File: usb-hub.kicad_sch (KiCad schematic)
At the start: 17 parts, among them U5 CH334P, Y2 X322512MSB4SI

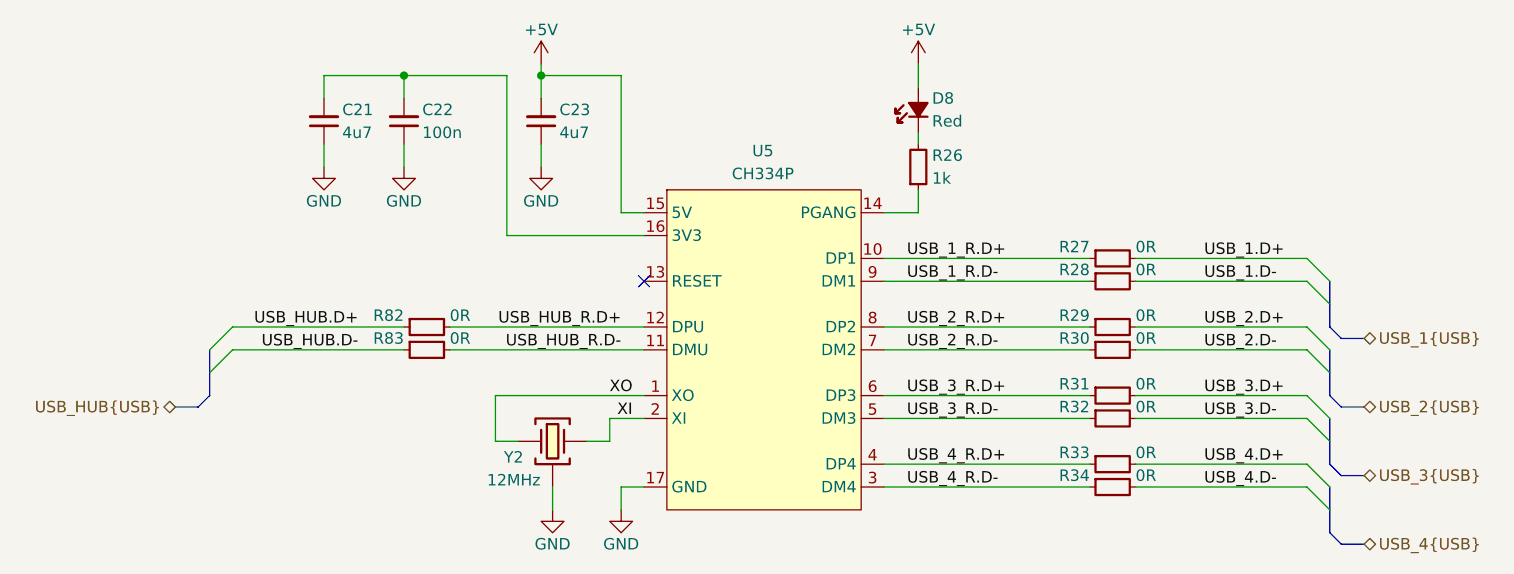
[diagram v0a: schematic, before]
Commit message: [#3] WIP: Clear ERC, re-annotate schematic
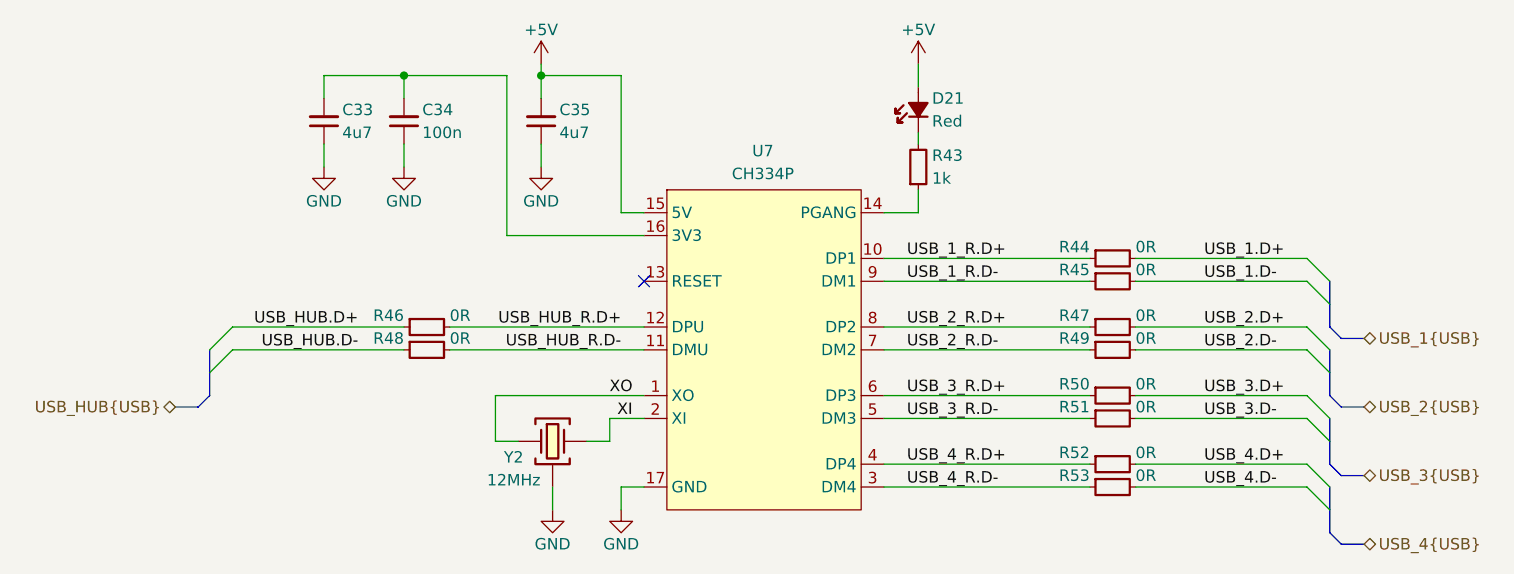
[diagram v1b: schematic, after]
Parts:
- renumbered C21 to C33, C22 to C34, C23 to C35, D8 to D21, R26 to R43, R27 to R44, R28 to R45, R82 to R46, R29 to R47, R83 to R48, R30 to R49, R31 to R50, R32 to R51, R33 to R52, R34 to R53, U5 to U7
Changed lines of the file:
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@@
 		(on_board yes)
 		(dnp no)
-		(property "Reference" "D8"
+		(property "Reference" "D21"
 			(at 164.084 80.01 90)
 			(effects
@@
 			(project "cm5-module"
 				(path "/090a8e41-87a8-4fb1-998b-60a2c0dc4cee/4f95f4d3-6409-4bd0-9a25-1272a43f6549"
-					(reference "D8")
+					(reference "D21")
 					(unit 1)
 				)
@@
 		(on_board yes)
 		(dnp no)
-		(property "Reference" "U5"
+		(property "Reference" "U7"
 			(at 145.288 85.852 0)
 			(effects
@@
 			(project ""
 				(path "/090a8e41-87a8-4fb1-998b-60a2c0dc4cee/4f95f4d3-6409-4bd0-9a25-1272a43f6549"
-					(reference "U5")
+					(reference "U7")
 					(unit 1)
 				)
@@
 		(on_board yes)
 		(dnp no)
-		(property "Reference" "R32"
+		(property "Reference" "R51"
 			(at 181.61 114.3 0)
 			(effects
@@
 			(project "cm5-module"
 				(path "/090a8e41-87a8-4fb1-998b-60a2c0dc4cee/4f95f4d3-6409-4bd0-9a25-1272a43f6549"
-					(reference "R32")
+					(reference "R51")
 					(unit 1)
 				)
@@
 		(on_board yes)
 		(dnp no)
-		(property "Reference" "#PWR070"
+		(property "Reference" "#PWR0108"
 			(at 96.52 93.98 0)
 			(effects
@@
 			(project "cm5-module"
 				(path "/090a8e41-87a8-4fb1-998b-60a2c0dc4cee/4f95f4d3-6409-4bd0-9a25-1272a43f6549"
-					(reference "#PWR070")
+					(reference "#PWR0108")
 					(unit 1)
 				)
@@
 		(on_board yes)
 		(dnp no)
-		(property "Reference" "#PWR073"
+		(property "Reference" "#PWR0111"
 			(at 121.92 132.08 0)
 			(effects
@@
 			(project "cm5-module"
 				(path "/090a8e41-87a8-4fb1-998b-60a2c0dc4cee/4f95f4d3-6409-4bd0-9a25-1272a43f6549"
-					(reference "#PWR073")
+					(reference "#PWR0111")
 					(unit 1)
 				)
@@
 		(on_board yes)
 		(dnp no)
-		(property "Reference" "#PWR071"
+		(property "Reference" "#PWR0109"
 			(at 105.41 93.98 0)
 			(effects
@@
 			(project "cm5-module"
 				(path "/090a8e41-87a8-4fb1-998b-60a2c0dc4cee/4f95f4d3-6409-4bd0-9a25-1272a43f6549"
-					(reference "#PWR071")
+					(reference "#PWR0109")
 					(unit 1)
 				)
@@
 		(on_board yes)
 		(dnp no)
-		(property "Reference" "#PWR074"
+		(property "Reference" "#PWR0112"
 			(at 129.54 132.08 0)
 			(effects
@@
 			(project "cm5-module"
 				(path "/090a8e41-87a8-4fb1-998b-60a2c0dc4cee/4f95f4d3-6409-4bd0-9a25-1272a43f6549"
-					(reference "#PWR074")
+					(reference "#PWR0112")
 					(unit 1)
 				)
@@
 		(on_board yes)
 		(dnp no)
-		(property "Reference" "R29"
+		(property "Reference" "R47"
 			(at 181.61 104.14 0)
 			(effects
@@
 			(project "cm5-module"
 				(path "/090a8e41-87a8-4fb1-998b-60a2c0dc4cee/4f95f4d3-6409-4bd0-9a25-1272a43f6549"
-					(reference "R29")
+					(reference "R47")
 					(unit 1)
 				)
@@
 		(on_board yes)
 		(dnp no)
-		(property "Reference" "R34"
+		(property "Reference" "R53"
 			(at 181.61 121.92 0)
 			(effects
@@
 			(project "cm5-module"
 				(path "/090a8e41-87a8-4fb1-998b-60a2c0dc4cee/4f95f4d3-6409-4bd0-9a25-1272a43f6549"
-					(reference "R34")
+					(reference "R53")
 					(unit 1)
 				)
@@
 		(on_board yes)
 		(dnp no)
-		(property "Reference" "R26"
+		(property "Reference" "R43"
 			(at 164.084 86.36 90)
 			(effects
@@
 			(project "cm5-module"
 				(path "/090a8e41-87a8-4fb1-998b-60a2c0dc4cee/4f95f4d3-6409-4bd0-9a25-1272a43f6549"
-					(reference "R26")
+					(reference "R43")
 					(unit 1)
 				)
@@
 		(on_board yes)
 		(dnp no)
-		(property "Reference" "R28"
+		(property "Reference" "R45"
 			(at 181.61 99.06 0)
 			(effects
@@
 			(project "cm5-module"
 				(path "/090a8e41-87a8-4fb1-998b-60a2c0dc4cee/4f95f4d3-6409-4bd0-9a25-1272a43f6549"
-					(reference "R28")
+					(reference "R45")
 					(unit 1)
 				)
@@
 		(on_board yes)
 		(dnp no)
-		(property "Reference" "C22"
+		(property "Reference" "C34"
 			(at 107.442 81.28 90)
 			(effects
@@
 			(project "cm5-module"
 				(path "/090a8e41-87a8-4fb1-998b-60a2c0dc4cee/4f95f4d3-6409-4bd0-9a25-1272a43f6549"
-					(reference "C22")
+					(reference "C34")
 					(unit 1)
 				)
@@
 		(on_board yes)
 		(dnp no)
-		(property "Reference" "C23"
+		(property "Reference" "C35"
 			(at 122.682 81.28 90)
 			(effects
@@
 			(project ""
 				(path "/090a8e41-87a8-4fb1-998b-60a2c0dc4cee/4f95f4d3-6409-4bd0-9a25-1272a43f6549"
-					(reference "C23")
+					(reference "C35")
 					(unit 1)
 				)
@@
 		(on_board yes)
 		(dnp no)
-		(property "Reference" "C21"
+		(property "Reference" "C33"
 			(at 98.552 81.28 90)
 			(effects
@@
 			(project "cm5-module"
 				(path "/090a8e41-87a8-4fb1-998b-60a2c0dc4cee/4f95f4d3-6409-4bd0-9a25-1272a43f6549"
-					(reference "C21")
+					(reference "C33")
 					(unit 1)
 				)
@@
 		(on_board yes)
 		(dnp no)
-		(property "Reference" "#PWR069"
+		(property "Reference" "#PWR0107"
 			(at 162.56 80.01 0)
 			(effects
@@
 			(project "cm5-module"
 				(path "/090a8e41-87a8-4fb1-998b-60a2c0dc4cee/4f95f4d3-6409-4bd0-9a25-1272a43f6549"
-					(reference "#PWR069")
+					(reference "#PWR0107")
 					(unit 1)
 				)
@@
 		(on_board yes)
 		(dnp no)
-		(property "Reference" "R83"
+		(property "Reference" "R48"
 			(at 105.41 106.68 0)
 			(effects
@@
 			(project "cm5-module"
 				(path "/090a8e41-87a8-4fb1-998b-60a2c0dc4cee/4f95f4d3-6409-4bd0-9a25-1272a43f6549"
-					(reference "R83")
+					(reference "R48")
 					(unit 1)
 				)
@@
 		(on_board yes)
 		(dnp no)
-		(property "Reference" "R33"
+		(property "Reference" "R52"
 			(at 181.61 119.38 0)
 			(effects
@@
 			(project "cm5-module"
 				(path "/090a8e41-87a8-4fb1-998b-60a2c0dc4cee/4f95f4d3-6409-4bd0-9a25-1272a43f6549"
-					(reference "R33")
+					(reference "R52")
 					(unit 1)
 				)
@@
 		(on_board yes)
 		(dnp no)
-		(property "Reference" "R27"
+		(property "Reference" "R44"
 			(at 181.61 96.52 0)
 			(effects
@@
 			(project "cm5-module"
 				(path "/090a8e41-87a8-4fb1-998b-60a2c0dc4cee/4f95f4d3-6409-4bd0-9a25-1272a43f6549"
-					(reference "R27")
+					(reference "R44")
 					(unit 1)
 				)
@@
 		(on_board yes)
 		(dnp no)
-		(property "Reference" "R31"
+		(property "Reference" "R50"
 			(at 181.61 111.76 0)
 			(effects
@@
 			(project "cm5-module"
 				(path "/090a8e41-87a8-4fb1-998b-60a2c0dc4cee/4f95f4d3-6409-4bd0-9a25-1272a43f6549"
-					(reference "R31")
+					(reference "R50")
 					(unit 1)
 				)
@@
 		(on_board yes)
 		(dnp no)
-		(property "Reference" "#PWR068"
+		(property "Reference" "#PWR0106"
 			(at 120.65 80.01 0)
 			(effects
@@
 			(project "cm5-module"
 				(path "/090a8e41-87a8-4fb1-998b-60a2c0dc4cee/4f95f4d3-6409-4bd0-9a25-1272a43f6549"
-					(reference "#PWR068")
+					(reference "#PWR0106")
 					(unit 1)
 				)
@@
 		(on_board yes)
 		(dnp no)
-		(property "Reference" "R82"
+		(property "Reference" "R46"
 			(at 105.41 104.14 0)
 			(effects
@@
 			(project "cm5-module"
 				(path "/090a8e41-87a8-4fb1-998b-60a2c0dc4cee/4f95f4d3-6409-4bd0-9a25-1272a43f6549"
-					(reference "R82")
+					(reference "R46")
 					(unit 1)
 				)
@@
 		(on_board yes)
 		(dnp no)
-		(property "Reference" "#PWR072"
+		(property "Reference" "#PWR0110"
 			(at 120.65 93.98 0)
 			(effects
@@
 			(project "cm5-module"
 				(path "/090a8e41-87a8-4fb1-998b-60a2c0dc4cee/4f95f4d3-6409-4bd0-9a25-1272a43f6549"
-					(reference "#PWR072")
+					(reference "#PWR0110")
 					(unit 1)
 				)
@@
 		(on_board yes)
 		(dnp no)
-		(property "Reference" "R30"
+		(property "Reference" "R49"
 			(at 181.61 106.68 0)
 			(effects
@@
 			(project "cm5-module"
 				(path "/090a8e41-87a8-4fb1-998b-60a2c0dc4cee/4f95f4d3-6409-4bd0-9a25-1272a43f6549"
-					(reference "R30")
+					(reference "R49")
 					(unit 1)
 				)

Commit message: [#3] Re-annotate schematic
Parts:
- renumbered C33 to C56, C34 to C57, C35 to C58, D21 to D17, R43 to R53, R44 to R54, R45 to R55, R46 to R56, R47 to R57, R48 to R58, R49 to R59, R50 to R60, R51 to R61, R52 to R62, R53 to R63, U7 to U11
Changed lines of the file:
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@@
 		(on_board yes)
 		(dnp no)
-		(property "Reference" "D21"
+		(property "Reference" "D17"
 			(at 164.084 80.01 90)
 			(effects
@@
 			(project "cm5-module"
 				(path "/090a8e41-87a8-4fb1-998b-60a2c0dc4cee/4f95f4d3-6409-4bd0-9a25-1272a43f6549"
-					(reference "D21")
+					(reference "D17")
 					(unit 1)
 				)
@@
 		(on_board yes)
 		(dnp no)
-		(property "Reference" "U7"
+		(property "Reference" "U11"
 			(at 145.288 85.852 0)
 			(effects
@@
 			(project ""
 				(path "/090a8e41-87a8-4fb1-998b-60a2c0dc4cee/4f95f4d3-6409-4bd0-9a25-1272a43f6549"
-					(reference "U7")
+					(reference "U11")
 					(unit 1)
 				)
@@
 		(on_board yes)
 		(dnp no)
-		(property "Reference" "R51"
+		(property "Reference" "R61"
 			(at 181.61 114.3 0)
 			(effects
@@
 			(project "cm5-module"
 				(path "/090a8e41-87a8-4fb1-998b-60a2c0dc4cee/4f95f4d3-6409-4bd0-9a25-1272a43f6549"
-					(reference "R51")
+					(reference "R61")
 					(unit 1)
 				)
@@
 		(on_board yes)
 		(dnp no)
-		(property "Reference" "#PWR0108"
+		(property "Reference" "#PWR0133"
 			(at 96.52 93.98 0)
 			(effects
@@
 			(project "cm5-module"
 				(path "/090a8e41-87a8-4fb1-998b-60a2c0dc4cee/4f95f4d3-6409-4bd0-9a25-1272a43f6549"
-					(reference "#PWR0108")
+					(reference "#PWR0133")
 					(unit 1)
 				)
@@
 		(on_board yes)
 		(dnp no)
-		(property "Reference" "#PWR0111"
+		(property "Reference" "#PWR0136"
 			(at 121.92 132.08 0)
 			(effects
@@
 			(project "cm5-module"
 				(path "/090a8e41-87a8-4fb1-998b-60a2c0dc4cee/4f95f4d3-6409-4bd0-9a25-1272a43f6549"
-					(reference "#PWR0111")
+					(reference "#PWR0136")
 					(unit 1)
 				)
@@
 		(on_board yes)
 		(dnp no)
-		(property "Reference" "#PWR0109"
+		(property "Reference" "#PWR0134"
 			(at 105.41 93.98 0)
 			(effects
@@
 			(project "cm5-module"
 				(path "/090a8e41-87a8-4fb1-998b-60a2c0dc4cee/4f95f4d3-6409-4bd0-9a25-1272a43f6549"
-					(reference "#PWR0109")
+					(reference "#PWR0134")
 					(unit 1)
 				)
@@
 		(on_board yes)
 		(dnp no)
-		(property "Reference" "#PWR0112"
+		(property "Reference" "#PWR0137"
 			(at 129.54 132.08 0)
 			(effects
@@
 			(project "cm5-module"
 				(path "/090a8e41-87a8-4fb1-998b-60a2c0dc4cee/4f95f4d3-6409-4bd0-9a25-1272a43f6549"
-					(reference "#PWR0112")
+					(reference "#PWR0137")
 					(unit 1)
 				)
@@
 		(on_board yes)
 		(dnp no)
-		(property "Reference" "R47"
+		(property "Reference" "R57"
 			(at 181.61 104.14 0)
 			(effects
@@
 			(project "cm5-module"
 				(path "/090a8e41-87a8-4fb1-998b-60a2c0dc4cee/4f95f4d3-6409-4bd0-9a25-1272a43f6549"
-					(reference "R47")
+					(reference "R57")
 					(unit 1)
 				)
@@
 		(on_board yes)
 		(dnp no)
-		(property "Reference" "R53"
+		(property "Reference" "R63"
 			(at 181.61 121.92 0)
 			(effects
@@
 			(project "cm5-module"
 				(path "/090a8e41-87a8-4fb1-998b-60a2c0dc4cee/4f95f4d3-6409-4bd0-9a25-1272a43f6549"
-					(reference "R53")
+					(reference "R63")
 					(unit 1)
 				)
@@
 		(on_board yes)
 		(dnp no)
-		(property "Reference" "R43"
+		(property "Reference" "R53"
 			(at 164.084 86.36 90)
 			(effects
@@
 			(project "cm5-module"
 				(path "/090a8e41-87a8-4fb1-998b-60a2c0dc4cee/4f95f4d3-6409-4bd0-9a25-1272a43f6549"
-					(reference "R43")
+					(reference "R53")
 					(unit 1)
 				)
@@
 		(on_board yes)
 		(dnp no)
-		(property "Reference" "R45"
+		(property "Reference" "R55"
 			(at 181.61 99.06 0)
 			(effects
@@
 			(project "cm5-module"
 				(path "/090a8e41-87a8-4fb1-998b-60a2c0dc4cee/4f95f4d3-6409-4bd0-9a25-1272a43f6549"
-					(reference "R45")
+					(reference "R55")
 					(unit 1)
 				)
@@
 		(on_board yes)
 		(dnp no)
-		(property "Reference" "C34"
+		(property "Reference" "C57"
 			(at 107.442 81.28 90)
 			(effects
@@
 			(project "cm5-module"
 				(path "/090a8e41-87a8-4fb1-998b-60a2c0dc4cee/4f95f4d3-6409-4bd0-9a25-1272a43f6549"
-					(reference "C34")
+					(reference "C57")
 					(unit 1)
 				)
@@
 		(on_board yes)
 		(dnp no)
-		(property "Reference" "C35"
+		(property "Reference" "C58"
 			(at 122.682 81.28 90)
 			(effects
@@
 			(project ""
 				(path "/090a8e41-87a8-4fb1-998b-60a2c0dc4cee/4f95f4d3-6409-4bd0-9a25-1272a43f6549"
-					(reference "C35")
+					(reference "C58")
 					(unit 1)
 				)
@@
 		(on_board yes)
 		(dnp no)
-		(property "Reference" "C33"
+		(property "Reference" "C56"
 			(at 98.552 81.28 90)
 			(effects
@@
 			(project "cm5-module"
 				(path "/090a8e41-87a8-4fb1-998b-60a2c0dc4cee/4f95f4d3-6409-4bd0-9a25-1272a43f6549"
-					(reference "C33")
+					(reference "C56")
 					(unit 1)
 				)
@@
 		(on_board yes)
 		(dnp no)
-		(property "Reference" "#PWR0107"
+		(property "Reference" "#PWR0132"
 			(at 162.56 80.01 0)
 			(effects
@@
 			(project "cm5-module"
 				(path "/090a8e41-87a8-4fb1-998b-60a2c0dc4cee/4f95f4d3-6409-4bd0-9a25-1272a43f6549"
-					(reference "#PWR0107")
+					(reference "#PWR0132")
 					(unit 1)
 				)
@@
 		(on_board yes)
 		(dnp no)
-		(property "Reference" "R48"
+		(property "Reference" "R58"
 			(at 105.41 106.68 0)
 			(effects
@@
 			(project "cm5-module"
 				(path "/090a8e41-87a8-4fb1-998b-60a2c0dc4cee/4f95f4d3-6409-4bd0-9a25-1272a43f6549"
-					(reference "R48")
+					(reference "R58")
 					(unit 1)
 				)
@@
 		(on_board yes)
 		(dnp no)
-		(property "Reference" "R52"
+		(property "Reference" "R62"
 			(at 181.61 119.38 0)
 			(effects
@@
 			(project "cm5-module"
 				(path "/090a8e41-87a8-4fb1-998b-60a2c0dc4cee/4f95f4d3-6409-4bd0-9a25-1272a43f6549"
-					(reference "R52")
+					(reference "R62")
 					(unit 1)
 				)
@@
 		(on_board yes)
 		(dnp no)
-		(property "Reference" "R44"
+		(property "Reference" "R54"
 			(at 181.61 96.52 0)
 			(effects
@@
 			(project "cm5-module"
 				(path "/090a8e41-87a8-4fb1-998b-60a2c0dc4cee/4f95f4d3-6409-4bd0-9a25-1272a43f6549"
-					(reference "R44")
+					(reference "R54")
 					(unit 1)
 				)
@@
 		(on_board yes)
 		(dnp no)
-		(property "Reference" "R50"
+		(property "Reference" "R60"
 			(at 181.61 111.76 0)
 			(effects
@@
 			(project "cm5-module"
 				(path "/090a8e41-87a8-4fb1-998b-60a2c0dc4cee/4f95f4d3-6409-4bd0-9a25-1272a43f6549"
-					(reference "R50")
+					(reference "R60")
 					(unit 1)
 				)
@@
 		(on_board yes)
 		(dnp no)
-		(property "Reference" "#PWR0106"
+		(property "Reference" "#PWR0131"
 			(at 120.65 80.01 0)
 			(effects
@@
 			(project "cm5-module"
 				(path "/090a8e41-87a8-4fb1-998b-60a2c0dc4cee/4f95f4d3-6409-4bd0-9a25-1272a43f6549"
-					(reference "#PWR0106")
+					(reference "#PWR0131")
 					(unit 1)
 				)
@@
 		(on_board yes)
 		(dnp no)
-		(property "Reference" "R46"
+		(property "Reference" "R56"
 			(at 105.41 104.14 0)
 			(effects
@@
 			(project "cm5-module"
 				(path "/090a8e41-87a8-4fb1-998b-60a2c0dc4cee/4f95f4d3-6409-4bd0-9a25-1272a43f6549"
-					(reference "R46")
+					(reference "R56")
 					(unit 1)
 				)
@@
 		(on_board yes)
 		(dnp no)
-		(property "Reference" "#PWR0110"
+		(property "Reference" "#PWR0135"
 			(at 120.65 93.98 0)
 			(effects
@@
 			(project "cm5-module"
 				(path "/090a8e41-87a8-4fb1-998b-60a2c0dc4cee/4f95f4d3-6409-4bd0-9a25-1272a43f6549"
-					(reference "#PWR0110")
+					(reference "#PWR0135")
 					(unit 1)
 				)
@@
 		(on_board yes)
 		(dnp no)
-		(property "Reference" "R49"
+		(property "Reference" "R59"
 			(at 181.61 106.68 0)
 			(effects
@@
 			(project "cm5-module"
 				(path "/090a8e41-87a8-4fb1-998b-60a2c0dc4cee/4f95f4d3-6409-4bd0-9a25-1272a43f6549"
-					(reference "R49")
+					(reference "R59")
 					(unit 1)
 				)
